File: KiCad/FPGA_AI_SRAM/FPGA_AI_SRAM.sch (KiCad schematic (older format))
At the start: 1 part

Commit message: paddle schematic done
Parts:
- added C1: 0.1uF, Capacitor_SMD:C_0805_2012Metric, symbol Device:C
- added J1, J2: Conn_01x22_Male, Connector_PinHeader_2.54mm:PinHeader_1x22_P2.54mm_Vertical, symbol Connector:Conn_01x22_Male
- gave numbers to parts that had none: 1
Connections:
- net at U1.1 (A15): now also J1.16 (Pin_16)
- net ~WE: now reaches U1.11 (~WE)
- net ~WE: now also J2.7 (Pin_7)
- net at U1.12 (CE2): now also J1.22 (Pin_22)
- net ~BHE: now reaches U1.14 (~BHE)
- net ~BHE: now also J2.4 (Pin_4)
- net ~BLE: now reaches U1.15 (~BLE)
- net ~BLE: now also J2.3 (Pin_3)
- net at U1.16 (A18): now also J1.19 (Pin_19)
- net at U1.17 (A17): now also J1.18 (Pin_18)
- net at U1.18 (A7): now also J1.8 (Pin_8)
- net at U1.19 (A6): now also J1.7 (Pin_7)
- net at U1.2 (A14): now also J1.15 (Pin_15)
- net at U1.20 (A5): now also J1.6 (Pin_6)
- net at U1.21 (A4): now also J1.5 (Pin_5)
- net at U1.22 (A3): now also J1.4 (Pin_4)
- net at U1.23 (A2): now also J1.3 (Pin_3)
- net at U1.24 (A1): now also J1.2 (Pin_2)
- net at U1.25 (A0): now also J1.1 (Pin_1)
- net at U1.26 (~CE1): now also J1.21 (Pin_21)
- net GND: now reaches U1.27 (VSS)
- net GND: now also U1.46 (VSS), C1.1, J2.1 (Pin_1)
- net ~OE: now reaches U1.28 (~OE)
- net ~OE: now also J2.6 (Pin_6)
- net at U1.29 (IO0): now also J2.22 (Pin_22)
- net at U1.3 (A13): now also J1.14 (Pin_14)
- net at U1.30 (IO8): now also J2.14 (Pin_14)
- net at U1.31 (IO1): now also J2.21 (Pin_21)
- net at U1.32 (IO9): now also J2.13 (Pin_13)
- net at U1.33 (IO2): now also J2.20 (Pin_20)
- net at U1.34 (IO10): now also J2.12 (Pin_12)
- net at U1.35 (IO3): now also J2.19 (Pin_19)
- net at U1.36 (IO11): now also J2.11 (Pin_11)
- net +3V3: now reaches U1.37 (VCC)
- net +3V3: now also C1.2, J2.2 (Pin_2)
- net at U1.38 (IO4): now also J2.18 (Pin_18)
- net at U1.39 (IO12): now also J2.10 (Pin_10)
- net at U1.4 (A12): now also J1.13 (Pin_13)
- net at U1.40 (IO5): now also J2.17 (Pin_17)
- net at U1.41 (IO13): now also J2.9 (Pin_9)
- net at U1.42 (IO6): now also J2.16 (Pin_16)
- net at U1.43 (IO14): now also J2.8 (Pin_8)
- net at U1.44 (IO7): now also J2.15 (Pin_15)
- net at U1.45 (A19/IO15): now also J1.20 (Pin_20)
- net ~BYTE: now reaches U1.47 (~BYTE)
- net ~BYTE: now also J2.5 (Pin_5)
- net at U1.48 (A16): now also J1.17 (Pin_17)
- net at U1.5 (A11): now also J1.12 (Pin_12)
- net at U1.6 (A10): now also J1.11 (Pin_11)
- net at U1.7 (A9): now also J1.10 (Pin_10)
- net at U1.8 (A8): now also J1.9 (Pin_9)
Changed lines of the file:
@@
 EELAYER 30 0
 EELAYER END
-$Descr A4 11693 8268
+$Descr USLetter 11000 8500
 encoding utf-8
 Sheet 1 1
-Title ""
+Title "8 Mbit SRAM Breadboard Adapter"
 Date ""
 Rev ""
@@
 $EndDescr
 $Comp
-L FPGA_AI_SRAM:CY62157 U?
+L Connector:Conn_01x22_Male J1
+U 1 1 5DEC4858
+P 3800 2450
+F 0 "J1" H 3908 3631 50  0000 C CNN
+F 1 "Conn_01x22_Male" H 3908 3540 50  0000 C CNN
+F 2 "Connector_PinHeader_2.54mm:PinHeader_1x22_P2.54mm_Vertical" H 3800 2450 50  0001 C CNN
+F 3 "~" H 3800 2450 50  0001 C CNN
+	1    3800 2450
+	1    0    0    -1
+$EndComp
+$Comp
+L Connector:Conn_01x22_Male J2
+U 1 1 5DECA18A
+P 6550 2750
+F 0 "J2" H 6522 2632 50  0000 R CNN
+F 1 "Conn_01x22_Male" H 6522 2723 50  0000 R CNN
+F 2 "Connector_PinHeader_2.54mm:PinHeader_1x22_P2.54mm_Vertical" H 6550 2750 50  0001 C CNN
+F 3 "~" H 6550 2750 50  0001 C CNN
+	1    6550 2750
+	-1   0    0    1
+$EndComp
+$Comp
+L Device:C C1
+U 1 1 5DEDCBD4
+P 5500 1250
+F 0 "C1" V 5248 1250 50  0000 C CNN
+F 1 "0.1uF" V 5339 1250 50  0000 C CNN
+F 2 "Capacitor_SMD:C_0805_2012Metric" H 5538 1100 50  0001 C CNN
+F 3 "~" H 5500 1250 50  0001 C CNN
+	1    5500 1250
+	0    1    1    0
+$EndComp
+$Comp
+L power:GND #PWR0101
+U 1 1 5DF1A464
+P 5100 4650
+F 0 "#PWR0101" H 5100 4400 50  0001 C CNN
+F 1 "GND" H 5105 4477 50  0000 C CNN
+F 2 "" H 5100 4650 50  0001 C CNN
+F 3 "" H 5100 4650 50  0001 C CNN
+	1    5100 4650
+	1    0    0    -1
+$EndComp
+Wire Wire Line
+	5000 4650 5100 4650
+Wire Wire Line
+	5100 4650 5200 4650
+Connection ~ 5100 4650
+$Comp
+L power:GND #PWR0102
+U 1 1 5DF1ED31
+P 5650 1300
+F 0 "#PWR0102" H 5650 1050 50  0001 C CNN
+F 1 "GND" H 5655 1127 50  0000 C CNN
+F 2 "" H 5650 1300 50  0001 C CNN
+F 3 "" H 5650 1300 50  0001 C CNN
+	1    5650 1300
+	1    0    0    -1
+$EndComp
+Wire Wire Line
+	5650 1250 5650 1300
+$Comp
+L power:+3.3V #PWR0103
+U 1 1 5DF21331
+P 5100 1200
+F 0 "#PWR0103" H 5100 1050 50  0001 C CNN
+F 1 "+3.3V" H 5115 1373 50  0000 C CNN
+F 2 "" H 5100 1200 50  0001 C CNN
+F 3 "" H 5100 1200 50  0001 C CNN
+	1    5100 1200
+	1    0    0    -1
+$EndComp
+Wire Wire Line
+	5100 1250 5350 1250
+$Comp
+L FPGA_AI_SRAM:CY62157 U1
 U 1 1 5DEC2ACD
 P 5100 2950
-F 0 "U?" H 5100 4031 50  0000 C CNN
+F 0 "U1" H 5100 4031 50  0000 C CNN
 F 1 "CY62157" H 5100 3940 50  0000 C CNN
 F 2 "Package_SO:TSOP-I-48_18.4x12mm_P0.5mm" H 5050 1750 50  0001 C CNN
@@
 	1    0    0    -1
 $EndComp
+Wire Wire Line
+	5100 1200 5100 1250
+Connection ~ 5100 1250
+Wire Wire Line
+	4000 1450 4650 1450
+Wire Wire Line
+	4650 1550 4000 1550
+Wire Wire Line
+	4000 1650 4650 1650
+Wire Wire Line
+	4650 1750 4000 1750
+Wire Wire Line
+	4000 1850 4650 1850
+Wire Wire Line
+	4650 1950 4000 1950
+Wire Wire Line
+	4650 2050 4000 2050
+Wire Wire Line
+	4000 2150 4650 2150
+Wire Wire Line
+	4650 2250 4000 2250
+Wire Wire Line
+	4000 2350 4650 2350
+Wire Wire Line
+	4650 2450 4000 2450
+Wire Wire Line
+	4000 2550 4650 2550
+Wire Wire Line
+	4650 2650 4000 2650
+Wire Wire Line
+	4000 2750 4650 2750
+Wire Wire Line
+	4650 2850 4000 2850
+Wire Wire Line
+	4000 2950 4650 2950
+Wire Wire Line
+	4000 3050 4650 3050
+Wire Wire Line
+	4650 3150 4000 3150
+Wire Wire Line
+	4000 3250 4650 3250
+Wire Wire Line
+	4650 3350 4000 3350
+Wire Wire Line
+	4650 4450 4000 4450
+Wire Wire Line
+	4000 4450 4000 3550
+Wire Wire Line
+	4650 4350 4100 4350
+Wire Wire Line
+	4100 4350 4100 3450
+Wire Wire Line
+	4100 3450 4000 3450
+Wire Wire Line
+	5550 1650 6350 1650
+Wire Wire Line
+	6350 1750 5550 1750
+Wire Wire Line
+	5550 1850 6350 1850
+Wire Wire Line
+	6350 1950 5550 1950
+Wire Wire Line
+	5550 2050 6350 2050
+Wire Wire Line
+	6350 2150 5550 2150
+Wire Wire Line
+	5550 2250 6350 2250
+Wire Wire Line
+	6350 2350 5550 2350
+Wire Wire Line
+	5550 2450 6350 2450
+Wire Wire Line
+	6350 2550 5550 2550
+Wire Wire Line
+	5550 2650 6350 2650
+Wire Wire Line
+	6350 2750 5550 2750
+Wire Wire Line
+	5550 2850 6350 2850
+Wire Wire Line
+	6350 2950 5550 2950
+Wire Wire Line
+	5550 3050 6350 3050
+Text GLabel 4600 3650 0    50   Input ~ 0
+~WE
+Text GLabel 4400 3750 0    50   Input ~ 0
+~OE
+Text GLabel 4600 3950 0    50   Input ~ 0
+~BYTE
+Text GLabel 4350 4050 0    50   Input ~ 0
+~BHE
+Text GLabel 4600 4150 0    50   Input ~ 0
+~BLE
+Text GLabel 6300 3150 0    50   Input ~ 0
+~WE
+Text GLabel 6050 3250 0    50   Input ~ 0
+~OE
+Text GLabel 6300 3350 0    50   Input ~ 0
+~BYTE
+Text GLabel 6050 3450 0    50   Input ~ 0
+~BHE
+Text GLabel 6300 3550 0    50   Input ~ 0
+~BLE
+$Comp
+L power:GND #PWR0104
+U 1 1 5DF45F96
+P 6300 3750
+F 0 "#PWR0104" H 6300 3500 50  0001 C CNN
+F 1 "GND" H 6305 3577 50  0000 C CNN
+F 2 "" H 6300 3750 50  0001 C CNN
+F 3 "" H 6300 3750 50  0001 C CNN
+	1    6300 3750
+	1    0    0    -1
+$EndComp
+$Comp
+L power:+3.3V #PWR0105
+U 1 1 5DF46338
+P 5700 3650
+F 0 "#PWR0105" H 5700 3500 50  0001 C CNN
+F 1 "+3.3V" H 5715 3823 50  0000 C CNN
+F 2 "" H 5700 3650 50  0001 C CNN
+F 3 "" H 5700 3650 50  0001 C CNN
+	1    5700 3650
+	1    0    0    -1
+$EndComp
+Wire Wire Line
+	6350 3150 6300 3150
+Wire Wire Line
+	6350 3250 6050 3250
+Wire Wire Line
+	6350 3350 6300 3350
+Wire Wire Line
+	6350 3450 6050 3450
+Wire Wire Line
+	6350 3550 6300 3550
+Wire Wire Line
+	6350 3650 5700 3650
+Wire Wire Line
+	6350 3750 6300 3750
+Wire Wire Line
+	4650 3650 4600 3650
+Wire Wire Line
+	4650 3750 4400 3750
+Wire Wire Line
+	4650 3950 4600 3950
+Wire Wire Line
+	4650 4050 4350 4050
+Wire Wire Line
+	4650 4150 4600 4150
 $EndSCHEMATC

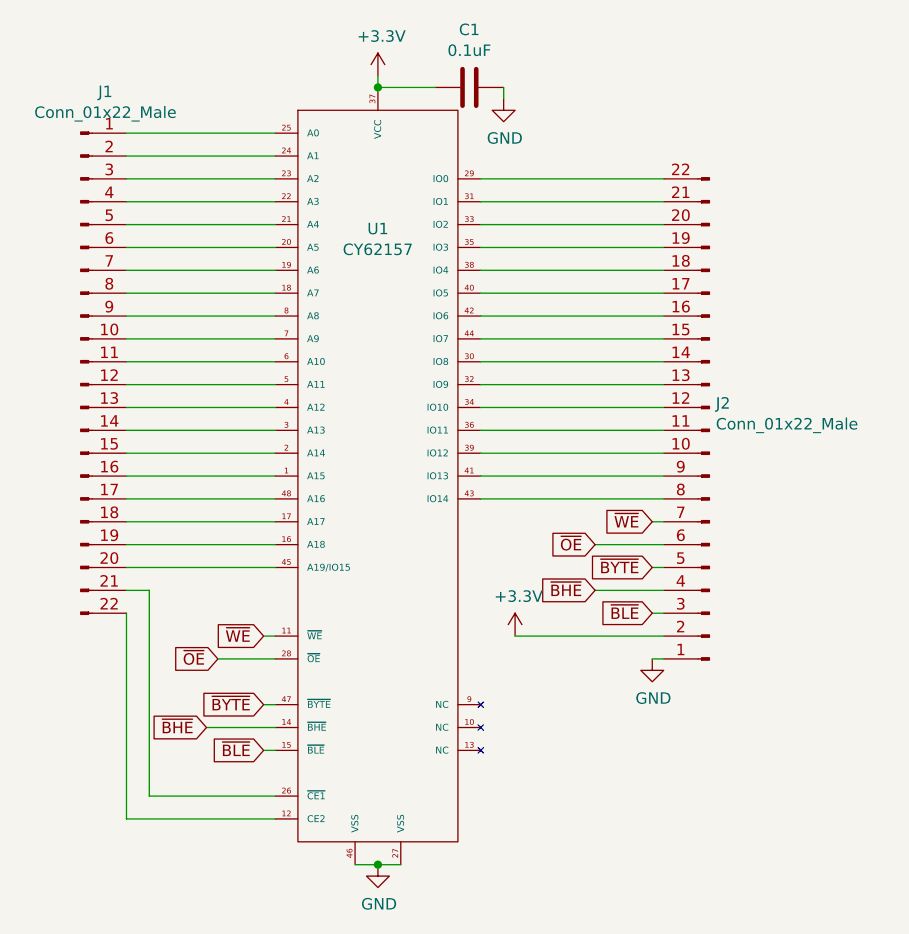
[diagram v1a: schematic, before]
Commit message: added net names
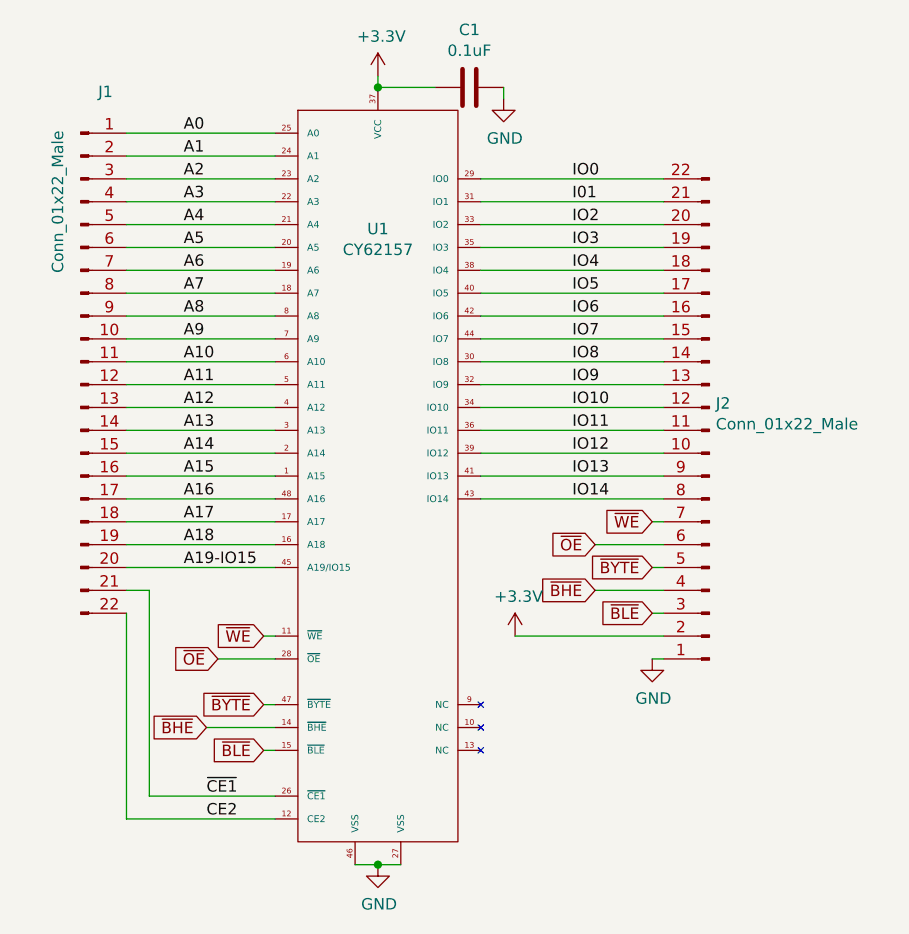
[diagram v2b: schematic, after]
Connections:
- net A15: now reaches J1.16 (Pin_16), U1.1 (A15)
- net CE2: now reaches J1.22 (Pin_22), U1.12 (CE2)
- net A18: now reaches J1.19 (Pin_19), U1.16 (A18)
- net A17: now reaches J1.18 (Pin_18), U1.17 (A17)
- net A7: now reaches J1.8 (Pin_8), U1.18 (A7)
- net A6: now reaches J1.7 (Pin_7), U1.19 (A6)
- net A14: now reaches J1.15 (Pin_15), U1.2 (A14)
- net A5: now reaches J1.6 (Pin_6), U1.20 (A5)
- net A4: now reaches J1.5 (Pin_5), U1.21 (A4)
- net A3: now reaches J1.4 (Pin_4), U1.22 (A3)
- net A2: now reaches J1.3 (Pin_3), U1.23 (A2)
- net A1: now reaches J1.2 (Pin_2), U1.24 (A1)
- net A0: now reaches J1.1 (Pin_1), U1.25 (A0)
- net ~CE1: now reaches J1.21 (Pin_21), U1.26 (~CE1)
- net IO0: now reaches J2.22 (Pin_22), U1.29 (IO0)
- net A13: now reaches J1.14 (Pin_14), U1.3 (A13)
- net IO8: now reaches J2.14 (Pin_14), U1.30 (IO8)
- net I01: now reaches J2.21 (Pin_21), U1.31 (IO1)
- net IO9: now reaches J2.13 (Pin_13), U1.32 (IO9)
- net IO2: now reaches J2.20 (Pin_20), U1.33 (IO2)
- net IO10: now reaches J2.12 (Pin_12), U1.34 (IO10)
- net IO3: now reaches J2.19 (Pin_19), U1.35 (IO3)
- net IO11: now reaches J2.11 (Pin_11), U1.36 (IO11)
- net IO4: now reaches J2.18 (Pin_18), U1.38 (IO4)
- net IO12: now reaches J2.10 (Pin_10), U1.39 (IO12)
- net A12: now reaches J1.13 (Pin_13), U1.4 (A12)
- net IO5: now reaches J2.17 (Pin_17), U1.40 (IO5)
- net IO13: now reaches J2.9 (Pin_9), U1.41 (IO13)
- net IO6: now reaches J2.16 (Pin_16), U1.42 (IO6)
- net IO14: now reaches J2.8 (Pin_8), U1.43 (IO14)
- net IO7: now reaches J2.15 (Pin_15), U1.44 (IO7)
- net A19-IO15: now reaches J1.20 (Pin_20), U1.45 (A19/IO15)
- net A16: now reaches J1.17 (Pin_17), U1.48 (A16)
- net A11: now reaches J1.12 (Pin_12), U1.5 (A11)
- net A10: now reaches J1.11 (Pin_11), U1.6 (A10)
- net A9: now reaches J1.10 (Pin_10), U1.7 (A9)
- net A8: now reaches J1.9 (Pin_9), U1.8 (A8)
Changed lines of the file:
@@
 P 3800 2450
 F 0 "J1" H 3908 3631 50  0000 C CNN
-F 1 "Conn_01x22_Male" H 3908 3540 50  0000 C CNN
+F 1 "Conn_01x22_Male" V 3700 3150 50  0000 C CNN
 F 2 "Connector_PinHeader_2.54mm:PinHeader_1x22_P2.54mm_Vertical" H 3800 2450 50  0001 C CNN
 F 3 "~" H 3800 2450 50  0001 C CNN
@@
 Wire Wire Line
 	4650 4150 4600 4150
+Text Label 5950 1650 0    50   ~ 0
+IO0
+Text Label 5950 1750 0    50   ~ 0
+I01
+Text Label 5950 1850 0    50   ~ 0
+IO2
+Text Label 5950 1950 0    50   ~ 0
+IO3
+Text Label 5950 2050 0    50   ~ 0
+IO4
+Text Label 5950 2150 0    50   ~ 0
+IO5
+Text Label 5950 2250 0    50   ~ 0
+IO6
+Text Label 5950 2350 0    50   ~ 0
+IO7
+Text Label 5950 2450 0    50   ~ 0
+IO8
+Text Label 5950 2550 0    50   ~ 0
+IO9
+Text Label 5950 2650 0    50   ~ 0
+IO10
+Text Label 5950 2750 0    50   ~ 0
+IO11
+Text Label 5950 2850 0    50   ~ 0
+IO12
+Text Label 5950 2950 0    50   ~ 0
+IO13
+Text Label 5950 3050 0    50   ~ 0
+IO14
+Text Label 4350 4350 0    50   ~ 0
+~CE1
+Text Label 4350 4450 0    50   ~ 0
+CE2
+Text Label 4250 3350 0    50   ~ 0
+A19-IO15
+Text Label 4250 3250 0    50   ~ 0
+A18
+Text Label 4250 3150 0    50   ~ 0
+A17
+Text Label 4250 3050 0    50   ~ 0
+A16
+Text Label 4250 2950 0    50   ~ 0
+A15
+Text Label 4250 2850 0    50   ~ 0
+A14
+Text Label 4250 2750 0    50   ~ 0
+A13
+Text Label 4250 2650 0    50   ~ 0
+A12
+Text Label 4250 2550 0    50   ~ 0
+A11
+Text Label 4250 2450 0    50   ~ 0
+A10
+Text Label 4250 2350 0    50   ~ 0
+A9
+Text Label 4250 2250 0    50   ~ 0
+A8
+Text Label 4250 2150 0    50   ~ 0
+A7
+Text Label 4250 2050 0    50   ~ 0
+A6
+Text Label 4250 1950 0    50   ~ 0
+A5
+Text Label 4250 1850 0    50   ~ 0
+A4
+Text Label 4250 1750 0    50   ~ 0
+A3
+Text Label 4250 1650 0    50   ~ 0
+A2
+Text Label 4250 1550 0    50   ~ 0
+A1
+Text Label 4250 1450 0    50   ~ 0
+A0
 $EndSCHEMATC
